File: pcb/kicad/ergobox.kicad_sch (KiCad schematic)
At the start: 80 parts, among them SW1 SW_Push, SW10 Kailh, SW11 Kailh, SW12 Kailh, SW13 Kailh, SW14 Kailh, SW15 Kailh, SW16 Kailh, SW17 Kailh, SW18 Kailh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

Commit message: feat: checkin milestone
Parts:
- C11: value 100n -> 1u
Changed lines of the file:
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@@
       (effects (font (size 1.27 1.27)) (justify left))
     )
-    (property "Value" "100n" (id 1) (at 157.48 54.6099 0)
+    (property "Value" "1u" (id 1) (at 157.48 54.6099 0)
       (effects (font (size 1.27 1.27)) (justify left))
     )
@@
     )
     (path "/8382cab1-0a9f-4a78-abaf-6794e075202c"
-      (reference "C11") (unit 1) (value "100n") (footprint "Capacitor_SMD:C_0402_1005Metric")
+      (reference "C11") (unit 1) (value "1u") (footprint "Capacitor_SMD:C_0402_1005Metric")
     )
     (path "/958e2596-6646-4fa3-8e5f-3a243fb25866"

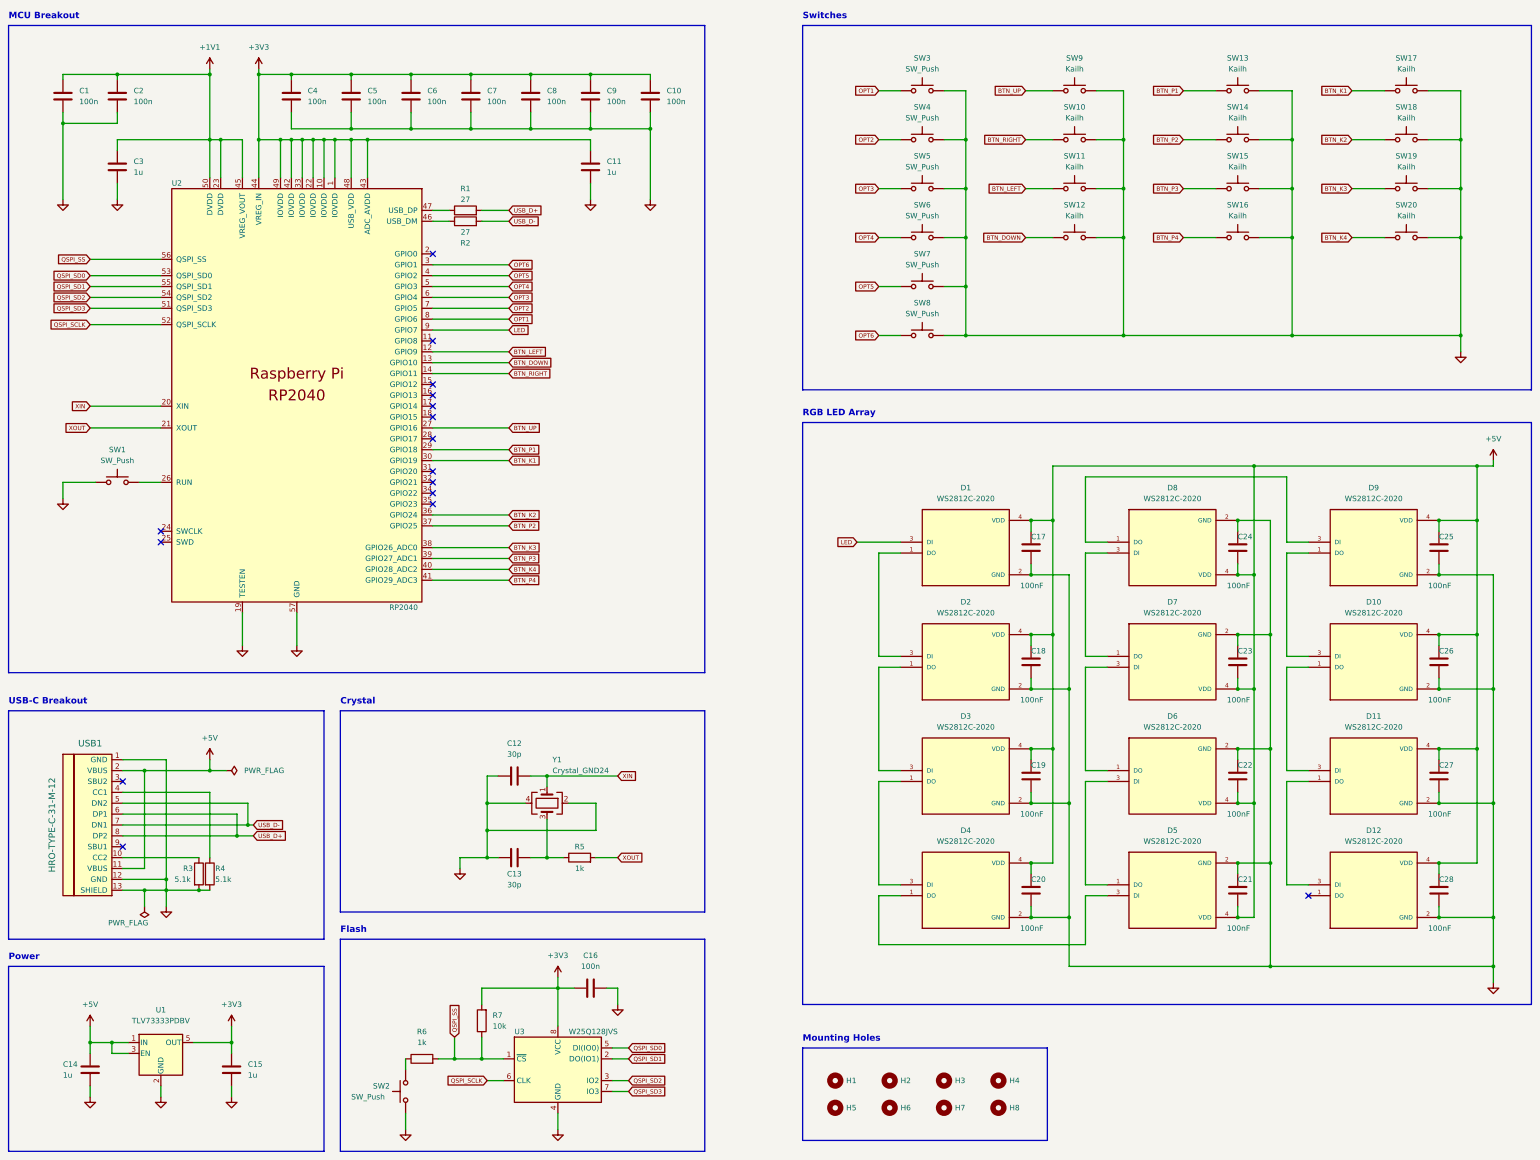
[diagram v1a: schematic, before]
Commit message: refactor: creates Ergobox v0.2 PCB design, with most SMD components on the underside
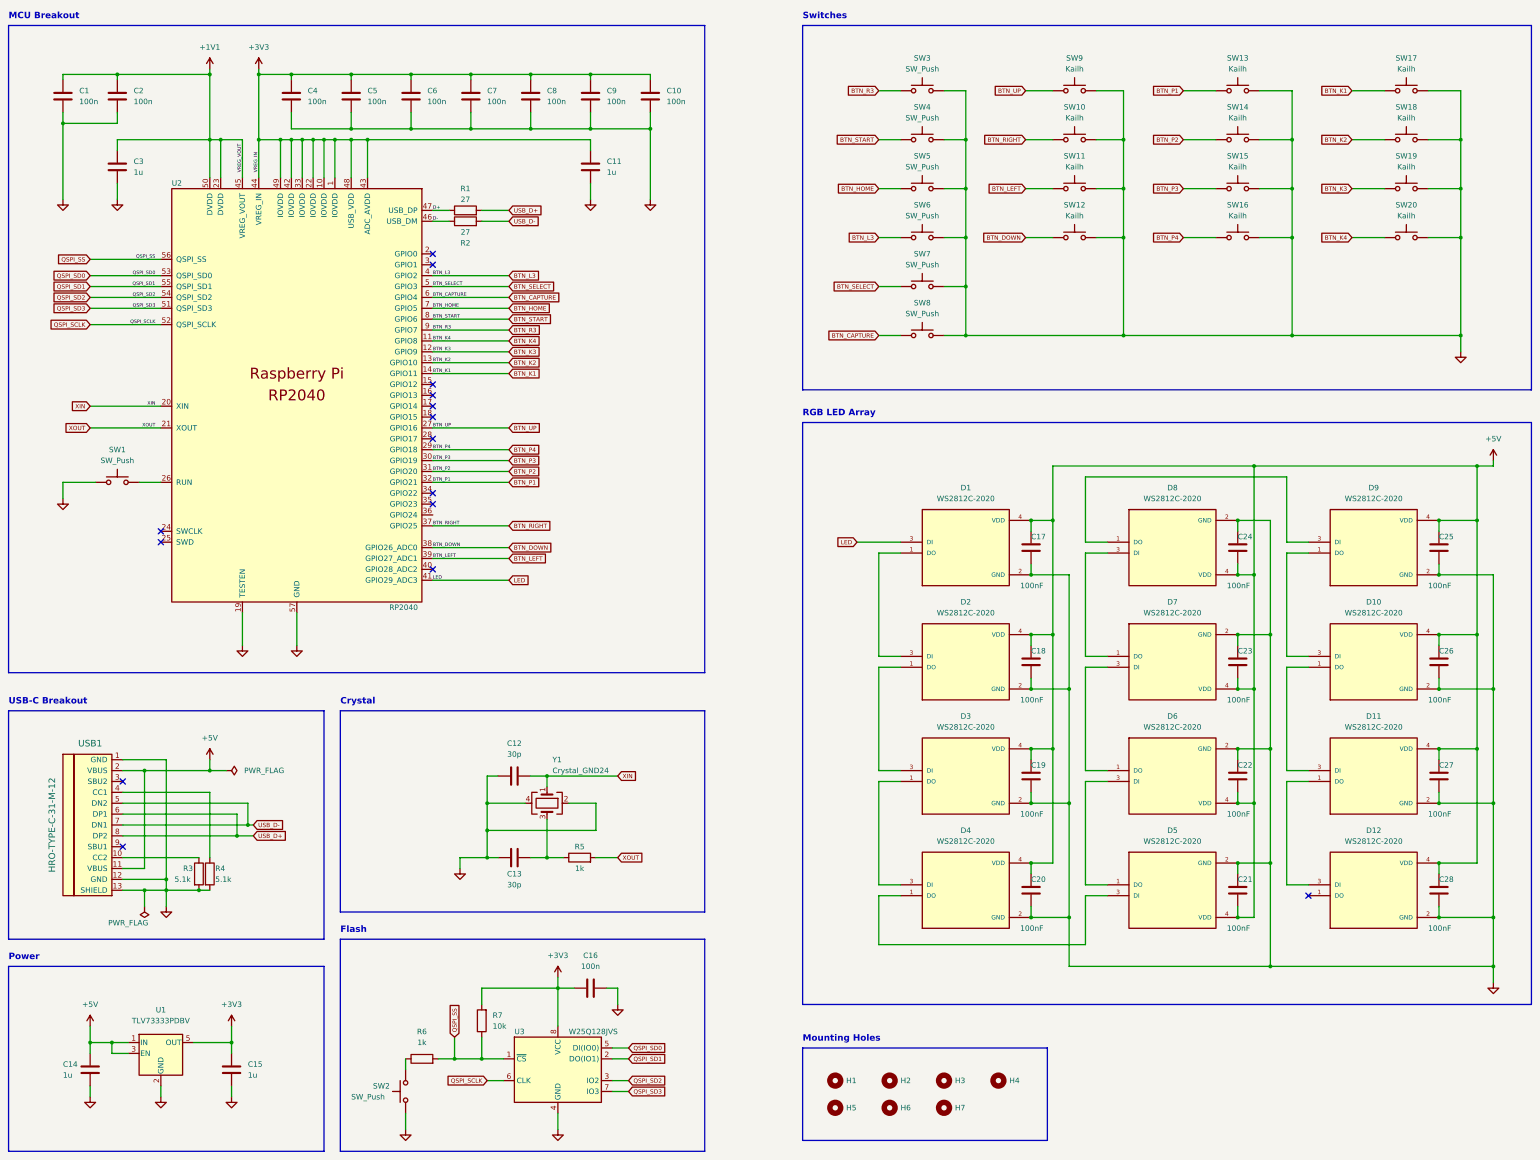
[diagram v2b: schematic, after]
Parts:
- removed H8: MountingHole, MountingHole:MountingHole_4.3mm_M4, symbol Mechanical:MountingHole
- H1, H2, H3, H4, H5, H6, H7: footprint MountingHole:MountingHole_4.3mm_M4 -> MountingHole:MountingHole_3.2mm_M3
- SW10, SW11, SW12, SW13, SW14, SW15, SW16, SW17, SW18, SW19, SW20, SW9: footprint Keyswitches:Kailh_socket_PG1350 -> Kailh Hotswap:SW_Hotswap_Kailh_Choc_V1V2
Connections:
- net BTN_DOWN: now also U2.38 (GPIO26_ADC0); no longer U2.13 (GPIO10)
- net BTN_K1: now also U2.14 (GPIO11); no longer U2.30 (GPIO19)
- net BTN_K2: now also U2.13 (GPIO10); no longer U2.36 (GPIO24)
- net BTN_K3: now also U2.12 (GPIO9); no longer U2.38 (GPIO26_ADC0)
- net BTN_K4: now also U2.11 (GPIO8); no longer U2.40 (GPIO28_ADC2)
- net BTN_LEFT: now also U2.39 (GPIO27_ADC1); no longer U2.12 (GPIO9)
- net BTN_P1: now also U2.32 (GPIO21); no longer U2.29 (GPIO18)
- net BTN_P2: now also U2.31 (GPIO20); no longer U2.37 (GPIO25)
- net BTN_P3: now also U2.30 (GPIO19); no longer U2.39 (GPIO27_ADC1)
- net BTN_P4: now also U2.29 (GPIO18); no longer U2.41 (GPIO29_ADC3)
- net BTN_RIGHT: now also U2.37 (GPIO25); no longer U2.14 (GPIO11)
- net LED: now also U2.41 (GPIO29_ADC3); no longer U2.9 (GPIO7)
- net D-: now reaches R2.1, U2.46 (USB_DM)
- net D+: now reaches R1.1, U2.47 (USB_DP)
- net OPT1 renamed BTN_R3
- net BTN_R3: now also U2.9 (GPIO7); no longer U2.8 (GPIO6)
- net OPT2 renamed BTN_HOME
- net BTN_HOME: now also SW5.1; no longer SW4.1
- net OPT3 renamed BTN_CAPTURE
- net BTN_CAPTURE: now also SW8.1; no longer SW5.1
- net OPT4 renamed BTN_L3
- net BTN_L3: now also U2.4 (GPIO2); no longer U2.5 (GPIO3)
- net OPT5 renamed BTN_SELECT
- net BTN_SELECT: now also U2.5 (GPIO3); no longer U2.4 (GPIO2)
- net OPT6: no longer names the net of U2.3 (GPIO1)
- net OPT6: no longer SW8.1
- new net BTN_START: SW4.1, U2.8 (GPIO6)
- no-connect marks 16 -> 15

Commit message: chore: adds JLCPCB part numbers to symbol fields
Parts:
- C1, C10, C16, C2, C4, C5, C6, C7, C8, C9: LCSC (none) -> C1525
- C11, C14, C15, C17, C18, C19, C20, C21, C22, C23, C24, C25, C26, C27, C28, C3: LCSC (none) -> C52923
- C12, C13: LCSC (none) -> C1570
- D1, D10, D11, D12, D2, D3, D4, D5, D6, D7, D8, D9: LCSC (none) -> C2976072
- R1, R2: LCSC (none) -> C138021
- R3, R4: LCSC (none) -> C25905
- R5, R6: LCSC (none) -> C11702
- R7: LCSC (none) -> C25744
- SW1, SW2: LCSC (none) -> C271750
- SW3, SW4, SW5, SW6, SW7, SW8: LCSC (none) -> C620304
- U1: LCSC (none) -> C134139
- U2: LCSC (none) -> C2040
- U3: LCSC (none) -> C97521
- USB1: LCSC (none) -> C165948
- Y1: LCSC (none) -> C9002

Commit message: chore: adjusts schematic and PCB metadata for BOM/POS export
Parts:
- C17, C18, C19, C20, C21, C22, C23, C24, C25, C26, C27, C28: value 100nF -> 100n
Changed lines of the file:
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@@
       (effects (font (size 1.27 1.27)) (justify left))
     )
-    (property "Value" "100nF" (id 1) (at 254 177.8 0)
+    (property "Value" "100n" (id 1) (at 254 177.8 0)
       (effects (font (size 1.27 1.27)) (justify left))
     )
@@
       (effects (font (size 1.27 1.27)) (justify left))
     )
-    (property "Value" "100nF" (id 1) (at 302.26 151.13 0)
+    (property "Value" "100n" (id 1) (at 302.26 151.13 0)
       (effects (font (size 1.27 1.27)) (justify left))
     )
@@
       (effects (font (size 1.27 1.27)) (justify left))
     )
-    (property "Value" "100nF" (id 1) (at 302.26 204.47 0)
+    (property "Value" "100n" (id 1) (at 302.26 204.47 0)
       (effects (font (size 1.27 1.27)) (justify left))
     )
@@
       (effects (font (size 1.27 1.27)) (justify left))
     )
-    (property "Value" "100nF" (id 1) (at 302.26 177.8 0)
+    (property "Value" "100n" (id 1) (at 302.26 177.8 0)
       (effects (font (size 1.27 1.27)) (justify left))
     )
@@
       (effects (font (size 1.27 1.27)) (justify left))
     )
-    (property "Value" "100nF" (id 1) (at 349.25 177.8 0)
+    (property "Value" "100n" (id 1) (at 349.25 177.8 0)
       (effects (font (size 1.27 1.27)) (justify left))
     )
@@
       (effects (font (size 1.27 1.27)) (justify left))
     )
-    (property "Value" "100nF" (id 1) (at 349.25 231.14 0)
+    (property "Value" "100n" (id 1) (at 349.25 231.14 0)
       (effects (font (size 1.27 1.27)) (justify left))
     )
@@
       (effects (font (size 1.27 1.27)) (justify left))
     )
-    (property "Value" "100nF" (id 1) (at 254 204.47 0)
+    (property "Value" "100n" (id 1) (at 254 204.47 0)
       (effects (font (size 1.27 1.27)) (justify left))
     )
@@
       (effects (font (size 1.27 1.27)) (justify left))
     )
-    (property "Value" "100nF" (id 1) (at 349.25 204.47 0)
+    (property "Value" "100n" (id 1) (at 349.25 204.47 0)
       (effects (font (size 1.27 1.27)) (justify left))
     )
@@
       (effects (font (size 1.27 1.27)) (justify left))
     )
-    (property "Value" "100nF" (id 1) (at 254 151.13 0)
+    (property "Value" "100n" (id 1) (at 254 151.13 0)
       (effects (font (size 1.27 1.27)) (justify left))
     )
@@
       (effects (font (size 1.27 1.27)) (justify left))
     )
-    (property "Value" "100nF" (id 1) (at 302.26 231.14 0)
+    (property "Value" "100n" (id 1) (at 302.26 231.14 0)
       (effects (font (size 1.27 1.27)) (justify left))
     )
@@
       (effects (font (size 1.27 1.27)) (justify left))
     )
-    (property "Value" "100nF" (id 1) (at 254 231.14 0)
+    (property "Value" "100n" (id 1) (at 254 231.14 0)
       (effects (font (size 1.27 1.27)) (justify left))
     )
@@
       (effects (font (size 1.27 1.27)) (justify left))
     )
-    (property "Value" "100nF" (id 1) (at 349.25 151.13 0)
+    (property "Value" "100n" (id 1) (at 349.25 151.13 0)
       (effects (font (size 1.27 1.27)) (justify left))
     )
@@
     )
     (path "/98d15ff8-10b7-4b06-9597-76ae169db16b"
-      (reference "C17") (unit 1) (value "100nF") (footprint "Capacitor_SMD:C_0402_1005Metric")
+      (reference "C17") (unit 1) (value "100n") (footprint "Capacitor_SMD:C_0402_1005Metric")
     )
     (path "/249be6c5-1b03-4dfc-87c2-5b2613e89c44"
-      (reference "C18") (unit 1) (value "100nF") (footprint "Capacitor_SMD:C_0402_1005Metric")
+      (reference "C18") (unit 1) (value "100n") (footprint "Capacitor_SMD:C_0402_1005Metric")
     )
     (path "/81fc6f57-de2f-4dab-8119-85bfae7ff4d0"
-      (reference "C19") (unit 1) (value "100nF") (footprint "Capacitor_SMD:C_0402_1005Metric")
+      (reference "C19") (unit 1) (value "100n") (footprint "Capacitor_SMD:C_0402_1005Metric")
     )
     (path "/c6eba513-b7ba-4b5f-a95e-bd0fad26fe86"
-      (reference "C20") (unit 1) (value "100nF") (footprint "Capacitor_SMD:C_0402_1005Metric")
+      (reference "C20") (unit 1) (value "100n") (footprint "Capacitor_SMD:C_0402_1005Metric")
     )
     (path "/aed7a51e-7018-4744-9ca7-fc18c5c6971b"
-      (reference "C21") (unit 1) (value "100nF") (footprint "Capacitor_SMD:C_0402_1005Metric")
+      (reference "C21") (unit 1) (value "100n") (footprint "Capacitor_SMD:C_0402_1005Metric")
     )
     (path "/3d3a48d9-0446-49e0-a6b1-5a4f01d78e1f"
-      (reference "C22") (unit 1) (value "100nF") (footprint "Capacitor_SMD:C_0402_1005Metric")
+      (reference "C22") (unit 1) (value "100n") (footprint "Capacitor_SMD:C_0402_1005Metric")
     )
     (path "/4f0ea93a-7c85-4bc1-8762-8ec79408d874"
-      (reference "C23") (unit 1) (value "100nF") (footprint "Capacitor_SMD:C_0402_1005Metric")
+      (reference "C23") (unit 1) (value "100n") (footprint "Capacitor_SMD:C_0402_1005Metric")
     )
     (path "/26f21666-c507-4f8e-8216-bb1090d4aaf3"
-      (reference "C24") (unit 1) (value "100nF") (footprint "Capacitor_SMD:C_0402_1005Metric")
+      (reference "C24") (unit 1) (value "100n") (footprint "Capacitor_SMD:C_0402_1005Metric")
     )
     (path "/da196ad1-0c6e-4810-9ba7-9b6800e78181"
-      (reference "C25") (unit 1) (value "100nF") (footprint "Capacitor_SMD:C_0402_1005Metric")
+      (reference "C25") (unit 1) (value "100n") (footprint "Capacitor_SMD:C_0402_1005Metric")
     )
     (path "/71c1e513-22f9-44df-b951-1bb36694f118"
-      (reference "C26") (unit 1) (value "100nF") (footprint "Capacitor_SMD:C_0402_1005Metric")
+      (reference "C26") (unit 1) (value "100n") (footprint "Capacitor_SMD:C_0402_1005Metric")
     )
     (path "/926ac79c-f1aa-4f1c-95a4-20fb111ca3be"
-      (reference "C27") (unit 1) (value "100nF") (footprint "Capacitor_SMD:C_0402_1005Metric")
+      (reference "C27") (unit 1) (value "100n") (footprint "Capacitor_SMD:C_0402_1005Metric")
     )
     (path "/7dc82d7d-0589-4395-b778-751c3d93ea8d"
-      (reference "C28") (unit 1) (value "100nF") (footprint "Capacitor_SMD:C_0402_1005Metric")
+      (reference "C28") (unit 1) (value "100n") (footprint "Capacitor_SMD:C_0402_1005Metric")
     )
     (path "/e8fdbe9d-e44e-44ec-8306-ec2dee4b73e1"

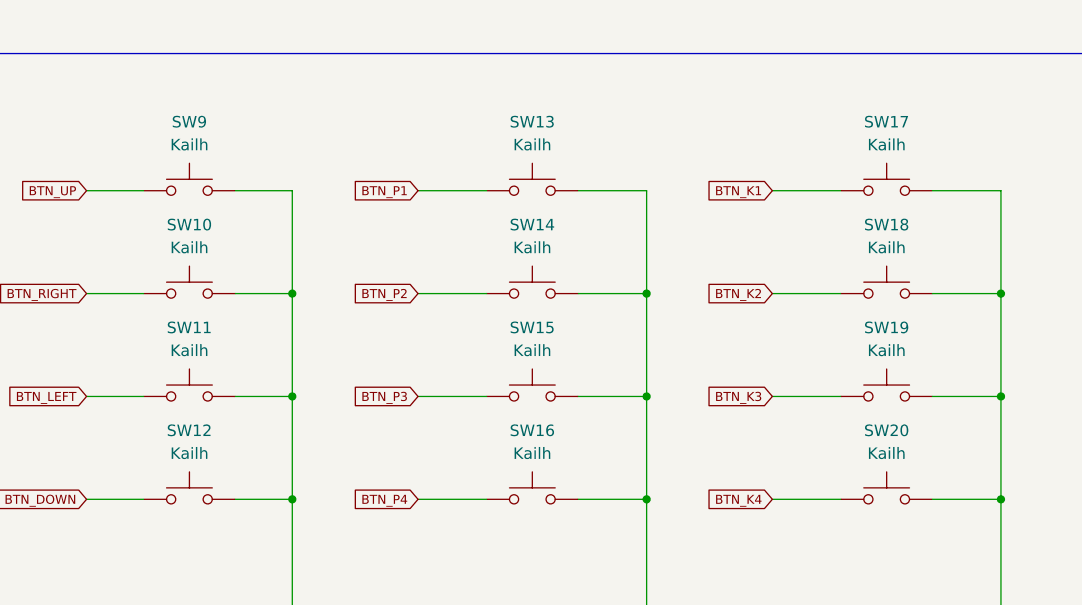
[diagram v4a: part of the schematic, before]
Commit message: chore: adds make command for generating pcb fab artifacts
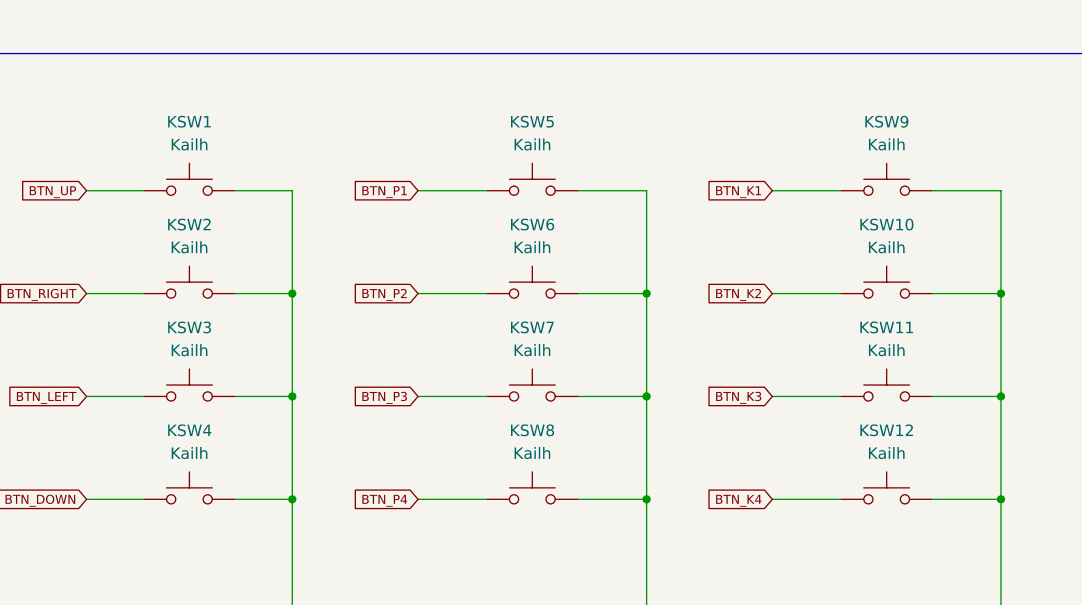
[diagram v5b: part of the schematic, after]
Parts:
- C8: JLCPCB_CORRECTION (none) -> 0;0;90
- KSW1: renamed from SW9; JLCPCB_IGNORE (none) -> true
- KSW10: renamed from SW18; JLCPCB_IGNORE (none) -> true
- KSW11: renamed from SW19; JLCPCB_IGNORE (none) -> true
- KSW12: renamed from SW20; JLCPCB_IGNORE (none) -> true
- KSW2: renamed from SW10; JLCPCB_IGNORE (none) -> true
- KSW3: renamed from SW11; JLCPCB_IGNORE (none) -> true
- KSW4: renamed from SW12; JLCPCB_IGNORE (none) -> true
- KSW5: renamed from SW13; JLCPCB_IGNORE (none) -> true
- KSW6: renamed from SW14; JLCPCB_IGNORE (none) -> true
- KSW7: renamed from SW15; JLCPCB_IGNORE (none) -> true
- KSW8: renamed from SW16; JLCPCB_IGNORE (none) -> true
- KSW9: renamed from SW17; JLCPCB_IGNORE (none) -> true
- U3: JLCPCB_CORRECTION (none) -> 0;0;-90
- USB1: JLCPCB_CORRECTION (none) -> 0;5.25;180
- Y1: JLCPCB_CORRECTION (none) -> 0;0;180
